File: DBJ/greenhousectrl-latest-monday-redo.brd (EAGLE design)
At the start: 73.6 x 69.5 mm, 56 parts, among them IC1 ATMEGA168TQFP-08, IC2 7824DT, IC4 L298, J1 POWER_JACKPTH, K2 G5LE, Q1 MMBT2222A, SW2 MOMENTARYBUTTON, X1 CRYSTALS-NOGND-HC49

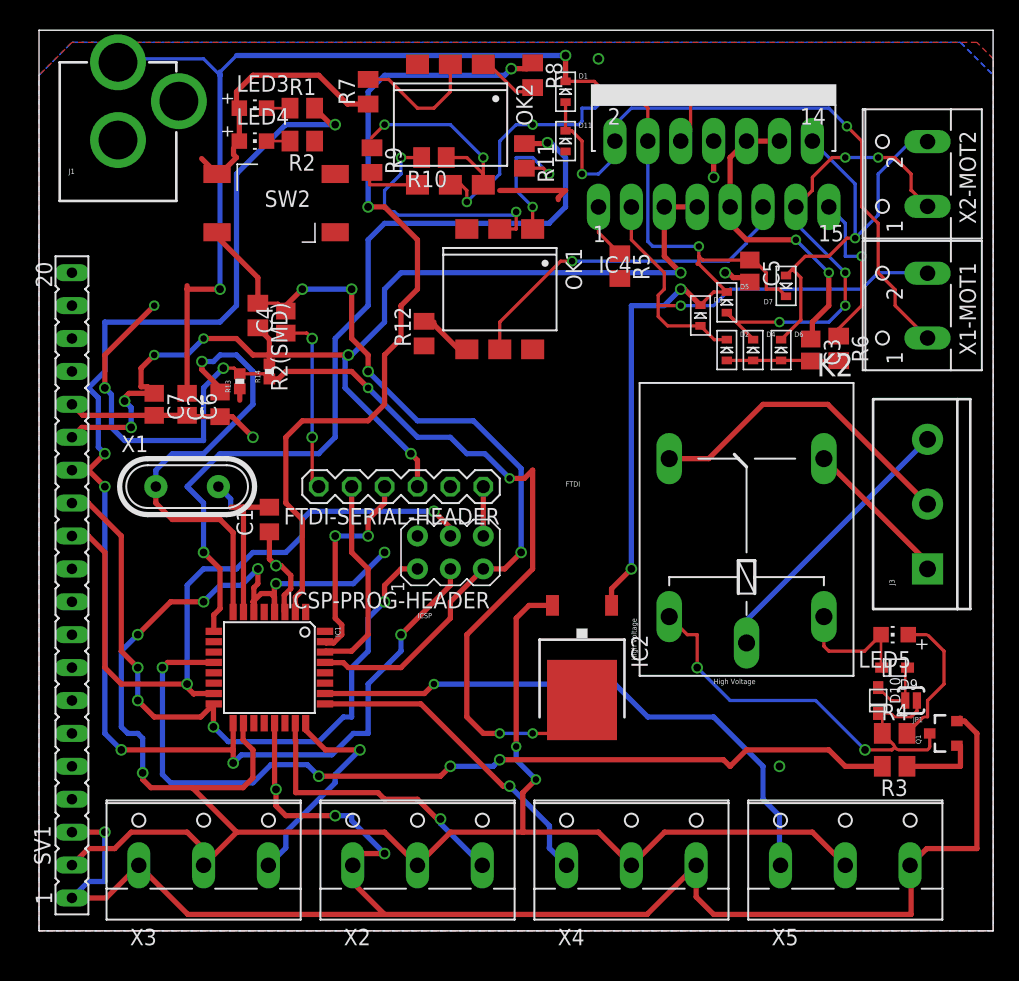
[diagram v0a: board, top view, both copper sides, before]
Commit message: Replaced 1x20 LCD with 2 1x8, gerb and DRC checked
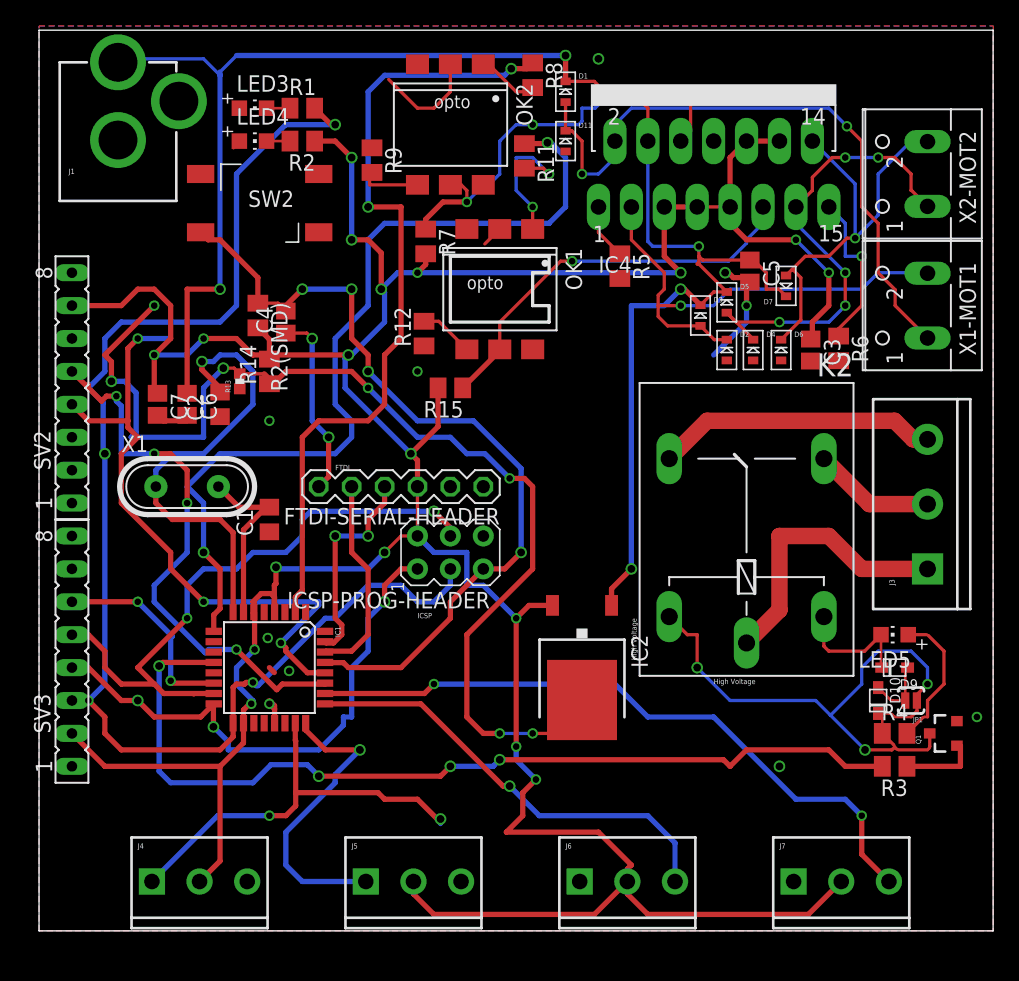
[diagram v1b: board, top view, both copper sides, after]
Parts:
- removed R10: (no value), adafruit:M0805
- removed SV1: (no value), con-lsta:FE20
- removed X2, X3, X4, X5: (no value), ece388:W237-103
- added J4, J5, J6, J7: (no value), SparkFun-Connectors:SCREWTERMINAL-3.5MM-3_LOCK.007S
- added R15: 1k, adafruit:M0805
- added SV2, SV3: (no value), con-lsta:FE08
- C1, C2: value (none) -> 20pF
- R1, R2: value (none) -> 150
- R11, R8: value (none) -> 240
- R12, R7, R9: value (none) -> 1k
- R13: value (none) -> 3k
- R14: value (none) -> 1k; device SparkFun-Resistors:0402-RES -> adafruit:M0805
- R2(SMD), R5, R6: value (none) -> 10k
- R3: value 1K -> 1k
- R4: value 1K -> 150
- moved R7 12.4 mm to (29.8, 53.2), turned to 270 degrees
- moved SW2 1.27 mm to (21.6, 58.4)
- moved C7 0.25 mm to (9.14, 40.6)
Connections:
- removed net ADC4: SV1.4
- removed net ADC5: SV1.5
- removed net N$4: OK2.2, R7.2
- removed net N$9: OK1.2, R10.2
- removed net SS: SV1.11
- net +5V: now also J4.2, J5.2, J6.2, J7.2, R15.2, R7.2, SV2.7, SV3.2; no longer SV1.15, SV1.2, X2.2, X3.2, X4.2, X5.2
- net COMMON: now also J3.1; no longer J3.3
- net ENA: now also R7.1
- net ENB: now also R15.1
- net GND: now also J4.3, J5.3, J6.1, J7.1, OK1.2, OK2.2, SV2.6, SV2.8, SV3.1; no longer R10.1, R7.1, SV1.1, SV1.16, SV1.3, X2.1, X3.1, X4.3, X5.3
- net MISO: now also SV3.4; no longer SV1.13
- net MOSI: now also SV3.5; no longer SV1.12
- net NC: now also J3.2; no longer J3.1
- net NO: now also J3.3; no longer J3.2
- net PB2: now also SV3.6
- net PC0: now also J4.1; no longer X2.3
- net PC1: now also J5.1; no longer X3.3
- net PC2: now also J6.3; no longer X4.1
- net PC3: now also J7.3; no longer X5.1
- net PC4: now also SV2.5
- net PC5: now also SV2.4
- net SCK: now also SV3.3; no longer SV1.14
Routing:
- net GND: track 209.5 -> 25.7 mm, vias 10 -> 8
- net PC5: track 0.00 -> 49.3 mm, vias 0 -> 3
- net PC4: track 0.00 -> 42.6 mm, vias 0 -> 4
- net N$9: track 19.5 -> 0.00 mm, vias 2 -> 0
- net +5V: track 259.3 -> 278.7 mm, vias 17 -> 18
- net PB2: track 0.00 -> 15.8 mm, vias 0 -> 2
- net COIL: track 34.0 -> 47.7 mm, vias 2 -> 3
- net MISO: track 52.9 -> 42.2 mm, vias 4 -> 3
- net PC0: track 22.3 -> 32.3 mm, vias 1 -> 2
- net N$4: track 9.90 -> 0.00 mm
- net PC2: track 24.9 -> 34.4 mm
- net PC3: track 44.9 -> 52.9 mm, vias 1 -> 2
- net PC1: track 17.2 -> 23.3 mm
- net MOSI: track 53.6 -> 47.9 mm
- net ENA: track 29.3 -> 33.8 mm
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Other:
- board text added: "opto"

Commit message: Fixed Orientation of Jack, New Gerb Files and Updated Folder for Viall
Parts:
- moved J1 16.2 mm to (7.24, 69.5), turned to 180 degrees
- moved SW2 0.64 mm to (22.2, 58.4)
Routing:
- net +12V: track 132.6 -> 132.0 mm
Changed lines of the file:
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@@
 </element>
 <element name="ICSP-PROG-HEADER" library="adafruit" package="AVRISP" value="AVRISP-6" x="31.75" y="29.21" rot="R90"/>
-<element name="J1" library="SparkFun-Connectors" package="POWER_JACK_PTH" value="POWER_JACKPTH" x="6.096" y="53.34">
-<attribute name="PROD_ID" value="CONN-08197" x="6.096" y="53.34" size="1.778" layer="27" display="off"/>
+<element name="J1" library="SparkFun-Connectors" package="POWER_JACK_PTH" value="POWER_JACKPTH" x="7.239" y="69.469" rot="R180">
+<attribute name="PROD_ID" value="CONN-08197" x="7.239" y="69.469" size="1.778" layer="27" rot="R180" display="off"/>
 </element>
 <element name="J3" library="SparkFun-Connectors" package="SCREWTERMINAL-5MM-3" value="" x="68.58" y="27.94" rot="R90">
@@
 <element name="C1" library="resistor" package="C0805" value="20pF" x="17.78" y="31.75" rot="R90"/>
 <element name="C2" library="resistor" package="C0805" value="20pF" x="13.97" y="40.64" rot="R90"/>
-<element name="SW2" library="ece388" package="SPST_NO_SMD" value="MOMENTARYBUTTON" x="21.59" y="58.42" rot="R180"/>
+<element name="SW2" library="ece388" package="SPST_NO_SMD" value="MOMENTARYBUTTON" x="22.225" y="58.42" rot="R180"/>
 <element name="K2" library="relay" package="G5LE" value="G5LE" x="54.61" y="31.75" rot="R90">
 <attribute name="OC_FARNELL" value="unknown" x="54.61" y="31.75" size="1.778" layer="27" ratio="15" rot="R90" display="off"/>
@@
 <wire x1="11.43" y1="49.53" x2="13.97" y2="49.53" width="0.4064" layer="1"/>
 <via x="13.97" y="49.53" extent="1-16" drill="0.6" shape="octagon"/>
-<wire x1="13.97" y1="49.53" x2="13.97" y2="66.04" width="0.4064" layer="16"/>
+<wire x1="13.97" y1="49.53" x2="13.97" y2="66.294" width="0.4064" layer="16"/>
 <wire x1="15.24" y1="67.564" x2="40.64" y2="67.564" width="0.4064" layer="16"/>
 <via x="40.64" y="67.564" extent="1-16" drill="0.6" shape="octagon"/>
@@
 <wire x1="45.72" y1="27.94" x2="44.19" y2="26.41" width="0.4064" layer="1"/>
 <wire x1="44.19" y1="26.41" x2="44.19" y2="25.12" width="0.4064" layer="1"/>
-<wire x1="13.97" y1="66.04" x2="12.7" y2="67.31" width="0.254" layer="16"/>
-<wire x1="12.7" y1="67.31" x2="7.89" y2="67.31" width="0.254" layer="16"/>
 <wire x1="43.65" y1="64.77" x2="45.72" y2="64.77" width="0.254" layer="1"/>
 <wire x1="45.72" y1="64.77" x2="46.99" y2="63.5" width="0.254" layer="1"/>
@@
 <wire x1="50.927" y1="52.832" x2="47.371" y2="52.832" width="0.254" layer="16"/>
 <wire x1="47.371" y1="52.832" x2="46.99" y2="53.213" width="0.254" layer="16"/>
-<wire x1="7.89" y1="67.31" x2="7.62" y2="67.04" width="0.254" layer="16"/>
-<wire x1="7.62" y1="67.04" x2="6.096" y2="67.04" width="0.254" layer="16"/>
 <wire x1="15.24" y1="67.564" x2="13.97" y2="66.294" width="0.254" layer="16"/>
-<wire x1="13.97" y1="66.294" x2="13.97" y2="66.04" width="0.4064" layer="16"/>
 <wire x1="57.658" y1="48.984" x2="57.112" y2="49.53" width="0.254" layer="1"/>
 <wire x1="57.112" y1="49.53" x2="56.134" y2="49.53" width="0.254" layer="1"/>
 <wire x1="56.134" y1="50.8" x2="55.157" y2="51.777" width="0.254" layer="1"/>
 <wire x1="55.157" y1="51.777" x2="54.864" y2="51.777" width="0.254" layer="1"/>
+<wire x1="11.43" y1="49.53" x2="11.43" y2="51.578" width="0.254" layer="1"/>
+<wire x1="11.43" y1="51.578" x2="7.239" y2="55.769" width="0.254" layer="1"/>
 </signal>
 <signal name="RST">
@@
 <wire x1="37.211" y1="35.687" x2="33.528" y2="39.37" width="0.4064" layer="16"/>
 <wire x1="13.97" y1="53.34" x2="13.0556" y2="53.34" width="0.4064" layer="1"/>
-<wire x1="13.0556" y1="53.34" x2="12.4714" y2="53.9242" width="0.4064" layer="1"/>
+<wire x1="13.0556" y1="53.34" x2="13.0556" y2="53.8734" width="0.254" layer="1"/>
+<wire x1="13.0556" y1="53.8734" x2="13.1064" y2="53.9242" width="0.254" layer="1"/>
 </signal>
 <signal name="SCK">
